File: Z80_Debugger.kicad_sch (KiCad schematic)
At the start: 28 parts, among them J1 ICSP, J2 UART, J3 I2C, J4 microSD, J5 CLK_SW, J6 M1_O, J7 USB_B_Mini, U1 Z84C00_PLCC, U2 PIC18F4520-xP, U3 AS6C4008-55PCN, U4 74HC138, U5 74AHC273, Y1 CXO_DIP14, Y2 Crystal

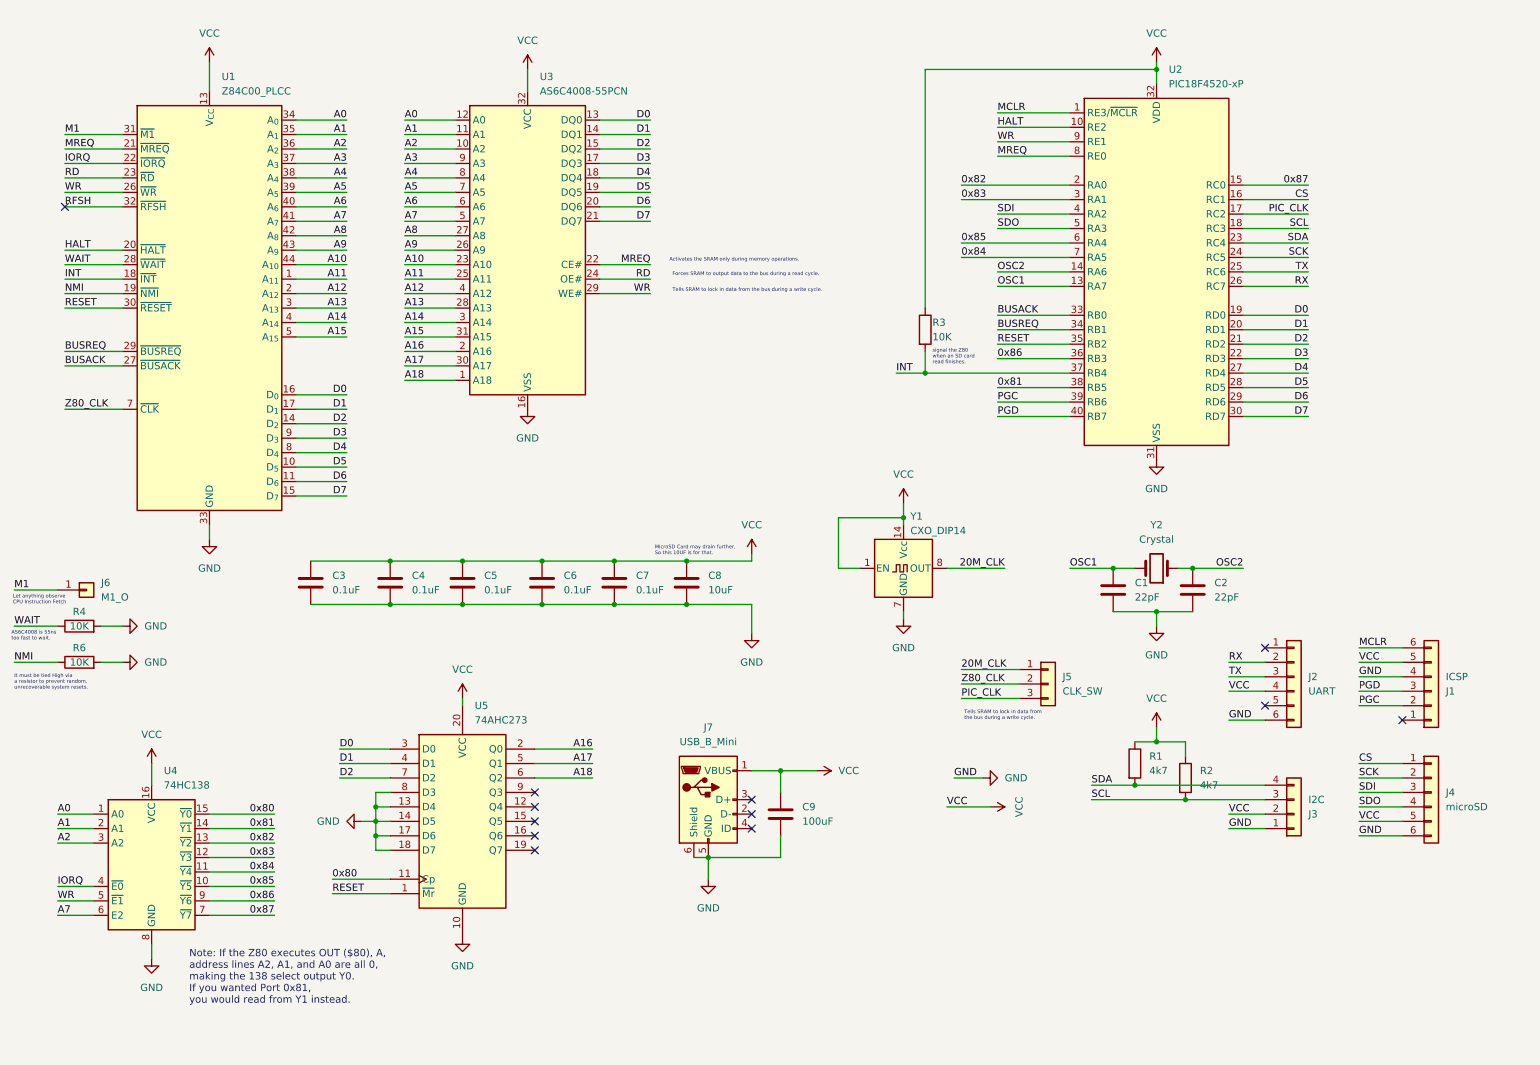
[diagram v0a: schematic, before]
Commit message: Rev1.1: Fix PUll-UPs pins
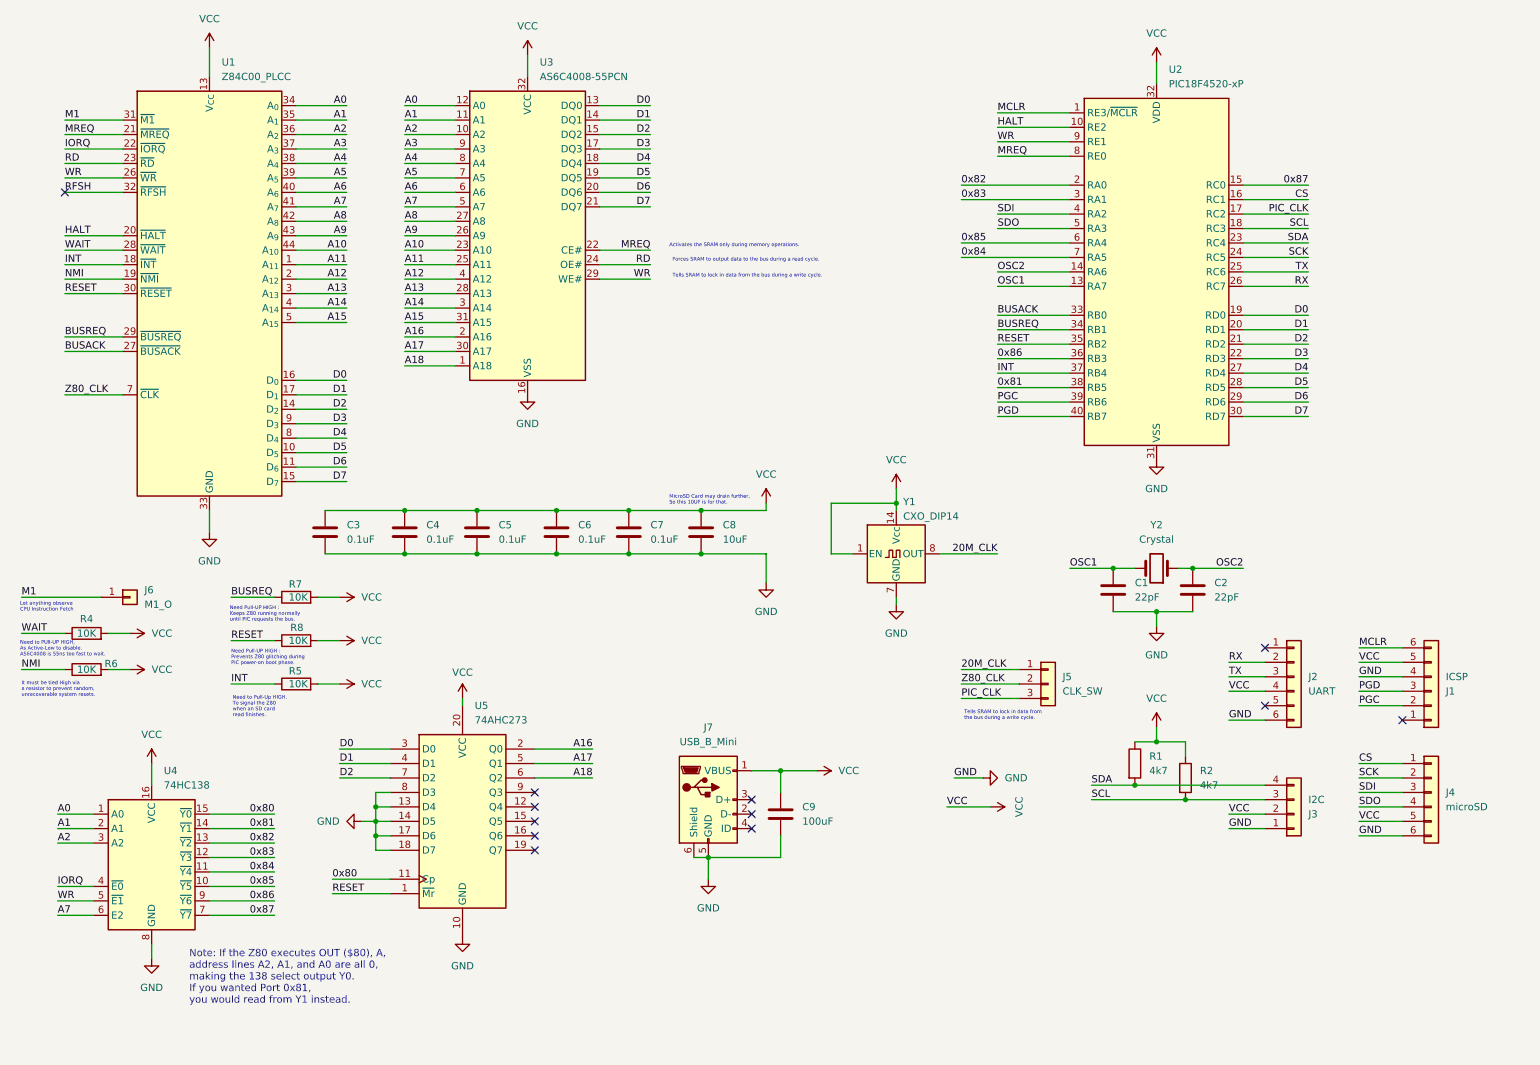
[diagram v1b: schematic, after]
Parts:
- removed R3: 10K, Resistor_THT:R_Axial_DIN0207_L6.3mm_D2.5mm_P10.16mm_Horizontal, symbol Device:R
- added R5, R7, R8: 10K, Resistor_THT:R_Axial_DIN0207_L6.3mm_D2.5mm_P10.16mm_Horizontal, symbol Device:R
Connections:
- net BUSREQ: now also R7.1
- net GND: no longer R4.2, R6.2
- net INT: now also R5.1
- net RESET: now also R8.1
- net VCC: now also R4.2, R6.2, R5.2, R7.2, R8.2
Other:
- note added: "Need Pull-UP HIGH : Keeps Z80 running normally until PIC requests the bus."
- note added: "Need Pull-UP HIGH : Prevents Z80 glitching during PIC power-on boot phase."
- note added: "Need to PUll-UP HIGH, As Active-Low to disable. AS6C4008 is 55ns too fast to wait."
- note added: "Need to Pull-Up HIGH. To signal the Z80 when an SD card read finishes."
- note removed: "AS6C4008 is 55ns too fast to wait."
- note removed: "signal the Z80 when an SD card read finishes."
- moved on the sheet: C3, C4, C5, C6, C7, C8, J6, R4, R6, U1, U3, Y1

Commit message: Refine SPI/MicroSD pins.
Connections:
- net SDI renamed MOSI
- net SDO renamed MISO
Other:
- note added: "Bit-bang SPI : RA2 -> MOSI RA3 -> MISO"
- title: (none) -> Z80 Debugger Rev1.1

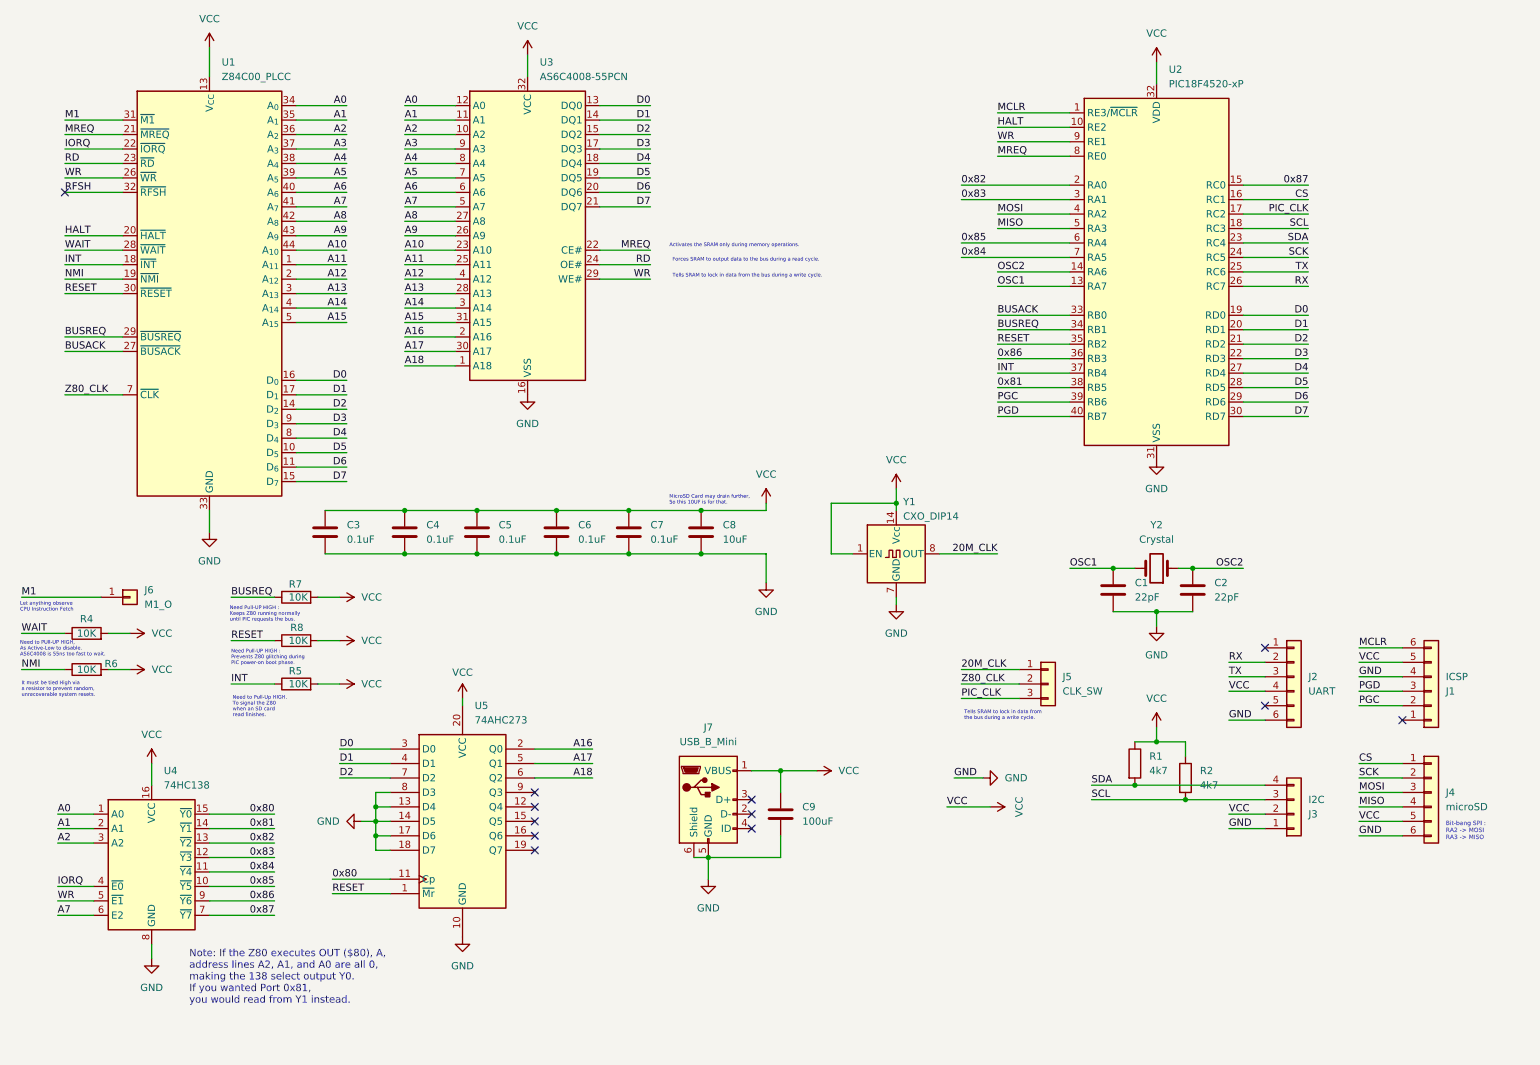
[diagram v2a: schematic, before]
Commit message: Rev.2: adding 3x74HC595
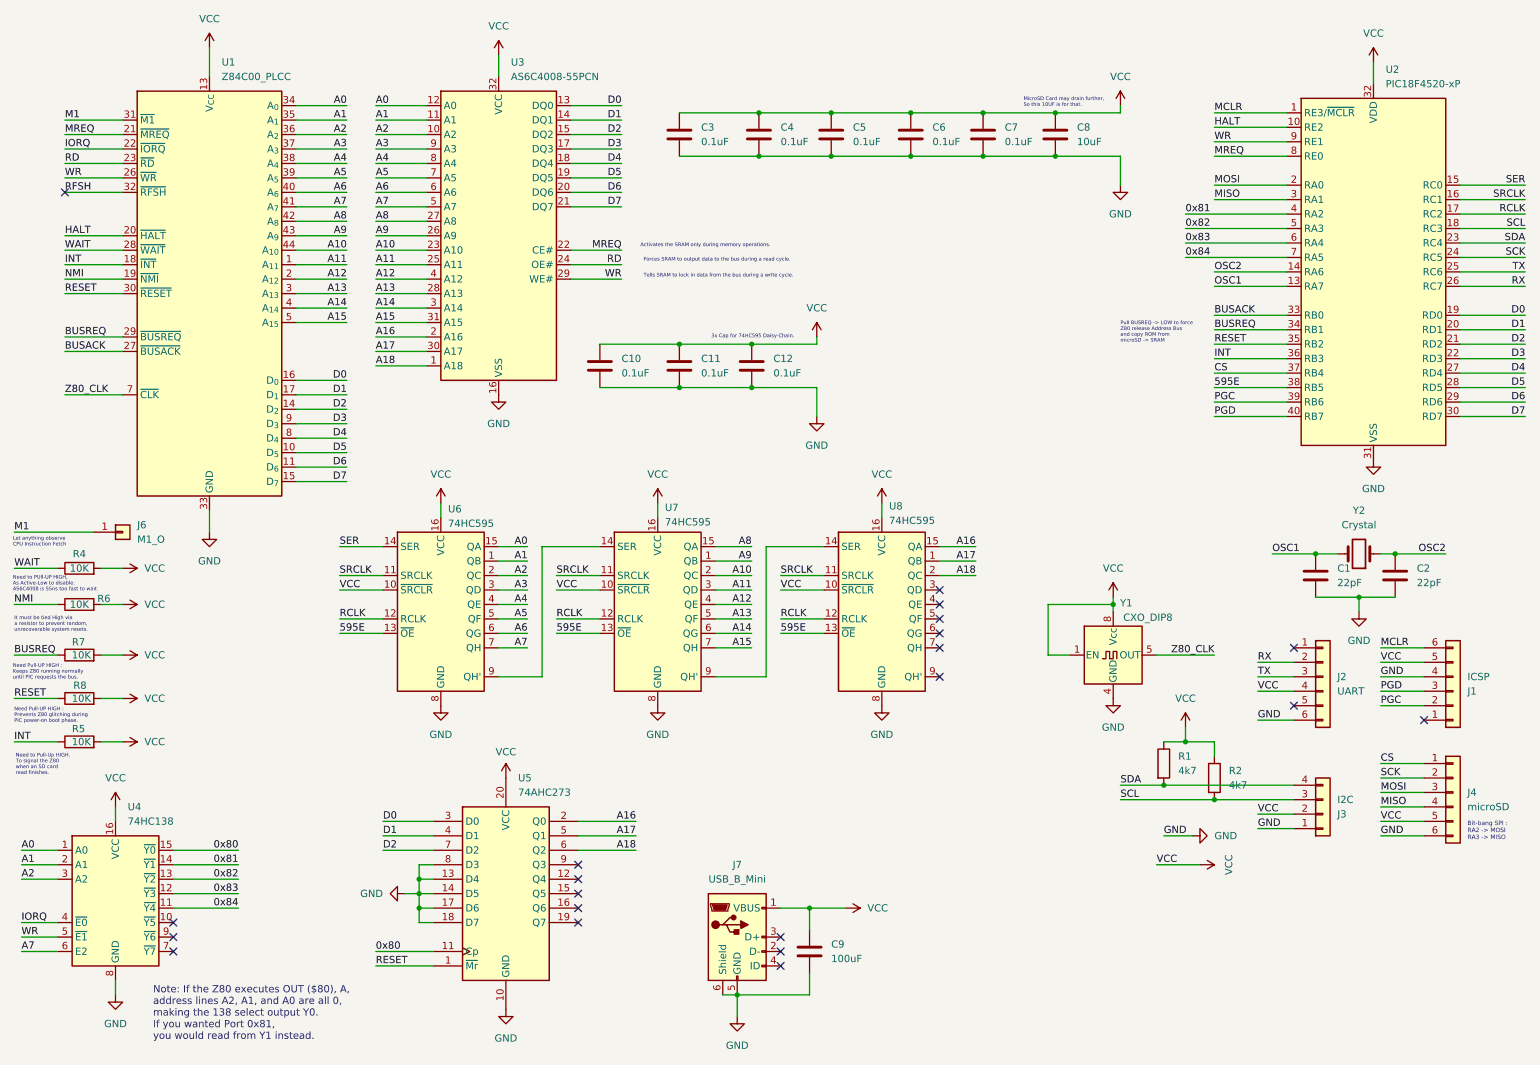
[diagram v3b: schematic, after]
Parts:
- removed J5: CLK_SW, Connector_PinHeader_2.54mm:PinHeader_1x03_P2.54mm_Vertical, symbol Connector_Generic:Conn_01x03
- added C10, C11, C12: 0.1uF, Capacitor_THT:C_Disc_D3.4mm_W2.1mm_P2.50mm, symbol Device:C
- added U6, U7, U8: 74HC595, Package_DIP:DIP-16_W7.62mm_Socket, symbol 74xx:74HC595
- Y1: value CXO_DIP14 -> CXO_DIP8; footprint Oscillator:Oscillator_DIP-14 -> Oscillator:Oscillator_DIP-8; symbol Oscillator:CXO_DIP14 -> Oscillator:CXO_DIP8
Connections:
- net 20M_CLK is gone; now on net VCC: Y1.8 (Vcc)
- net 0x81: now also U2.4 (RA2); no longer U2.38 (RB5)
- net 0x82: now also U2.5 (RA3); no longer U2.2 (RA0)
- net 0x83: now also U2.6 (RA4); no longer U2.3 (RA1)
- net A0: now also U6.15 (QA)
- net A1: now also U6.1 (QB)
- net A10: now also U7.2 (QC)
- net A11: now also U7.3 (QD)
- net A12: now also U7.4 (QE)
- net A13: now also U7.5 (QF)
- net A14: now also U7.6 (QG)
- net A15: now also U7.7 (QH)
- net A16: now also U8.15 (QA)
- net A17: now also U8.1 (QB)
- net A18: now also U8.2 (QC)
- net A2: now also U6.2 (QC)
- net A3: now also U6.3 (QD)
- net A4: now also U6.4 (QE)
- net A5: now also U6.5 (QF)
- net A6: now also U6.6 (QG)
- net A7: now also U6.7 (QH)
- net A8: now also U7.15 (QA)
- net A9: now also U7.1 (QB)
- net CS: now also U2.37 (RB4); no longer U2.16 (RC1)
- net GND: now also Y1.4 (GND), C10.1, C11.1, C12.1, U6.8 (GND), U7.8 (GND), U8.8 (GND); no longer Y1.7 (GND)
- net INT: now also U2.36 (RB3); no longer U2.37 (RB4)
- net MISO: now also U2.3 (RA1); no longer U2.5 (RA3)
- net MOSI: now also U2.2 (RA0); no longer U2.4 (RA2)
- net VCC: now also C10.2, C11.2, C12.2, U6.10 (~{SRCLR}), U6.16 (VCC), U7.10 (~{SRCLR}), U7.16 (VCC), U8.10 (~{SRCLR}), U8.16 (VCC); no longer Y1.14 (Vcc)
- net Z80_CLK: now also Y1.5 (OUT)
- net 0x85: no longer names the net of U4.10 (~{Y5})
- net 0x85: no longer U2.6 (RA4)
- net 0x86: no longer names the net of U4.9 (~{Y6})
- net 0x86: no longer U2.36 (RB3)
- net 0x87: no longer names the net of U4.7 (~{Y7})
- net 0x87: no longer U2.15 (RC0)
- net PIC_CLK renamed RCLK
- net RCLK: now also U6.12 (RCLK), U7.12 (RCLK), U8.12 (RCLK)
- new net: U6.9 (QH'), U7.14 (SER)
- new net: U7.9 (QH'), U8.14 (SER)
- new net 595E: U2.38 (RB5), U6.13 (~{OE}), U7.13 (~{OE}), U8.13 (~{OE})
- new net SER: U2.15 (RC0), U6.14 (SER)
- new net SRCLK: U2.16 (RC1), U6.11 (SRCLK), U7.11 (SRCLK), U8.11 (SRCLK)
- no-connect marks 12 -> 21
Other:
- note added: "3x Cap for 74HC595 Daisy-Chain."
- note added: "Pull BUSREQ -> LOW to force Z80 release Address Bus and copy ROM from microSD -> SRAM"
- moved on the sheet: C1, C2, C3, C4, C5, C6, C7, C8, C9, J1, J2, J3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
